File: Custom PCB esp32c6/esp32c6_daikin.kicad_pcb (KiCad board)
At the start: 2 copper layers, 31.6 x 19.8 mm, 35 parts, among them J2 Conn_01x05, Q1 BSS138PS, U1 TPS562246, U2 WT0132C6-S5

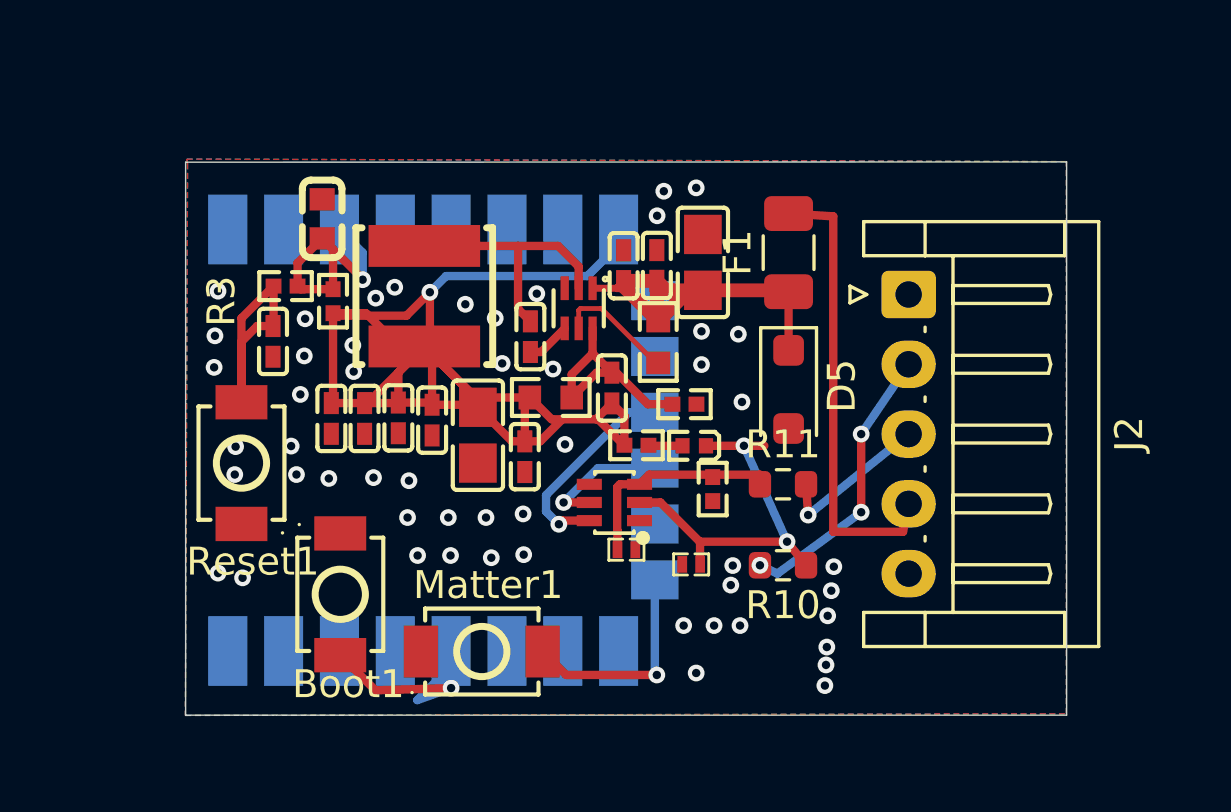
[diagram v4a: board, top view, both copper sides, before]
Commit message: feat(xiao-pcb): place XIAO + kept parts on grown outline
Sync the PCB to the reviewed XIAO-carrier schematic (Task 7, placement only;
routing is Task 8).

- Remove 12 footprints no longer in the netlist (Reset1, Boot1, Matter1, D4,
  R9, C1, C2, C4, C5, C6, C7, C8).
- Swap U2 from the old module footprint (easyeda2kicad:WT0132C6-S5) to the
  Seeed XIAO land pattern (Seeed_XIAO:XIAO-ESP32-C6-DIP).
- Add the 3 new parts: U2 XIAO, D6 (PMEG2005 VBUS Schottky, D_SOD-123),
  C20 (10uF XIAO VBUS decap), R12 (10k). No ferrite (dropped in schematic).
- Reassign every pad net from the exported netlist (89 pads, 0 mismatches,
  full ref-set parity).
- Grow the outline to 40x25 mm. Place U2 on B.Cu at the left short edge with
  the antenna end overhanging (~1mm) and a copper keep-out rule area (no
  tracks / no zone fills, F.Cu+B.Cu) under the antenna. Buck (U1+L1) far end,
  J2 on the right long edge, shifter (Q1/R10/R11) and protection (F1/D5/D6/
  D2/D3) placed accordingly. Courtyard-free R/C nest in the module center gap
  between the two castellated PTH pad rows.
- Delete the stale rev-b routing (209 tracks) and GND pour so the board is
  placed-not-routed.

D5 (SMF15A, unidirectional TVS in a bidirectional symbol): verified at board
level that pad 1 (cathode/band) lands on V_in and pad 2 on GND - correct
clamp polarity.

DRC (kicad-cli 10.0.4): zero footprint/courtyard-overlap, shorting, clearance
or edge-clearance errors; 49 unconnected items expected pre-routing. Remaining
warnings are silkscreen crowding and pre-existing easyeda2kicad lib-table
entries, both non-gating.
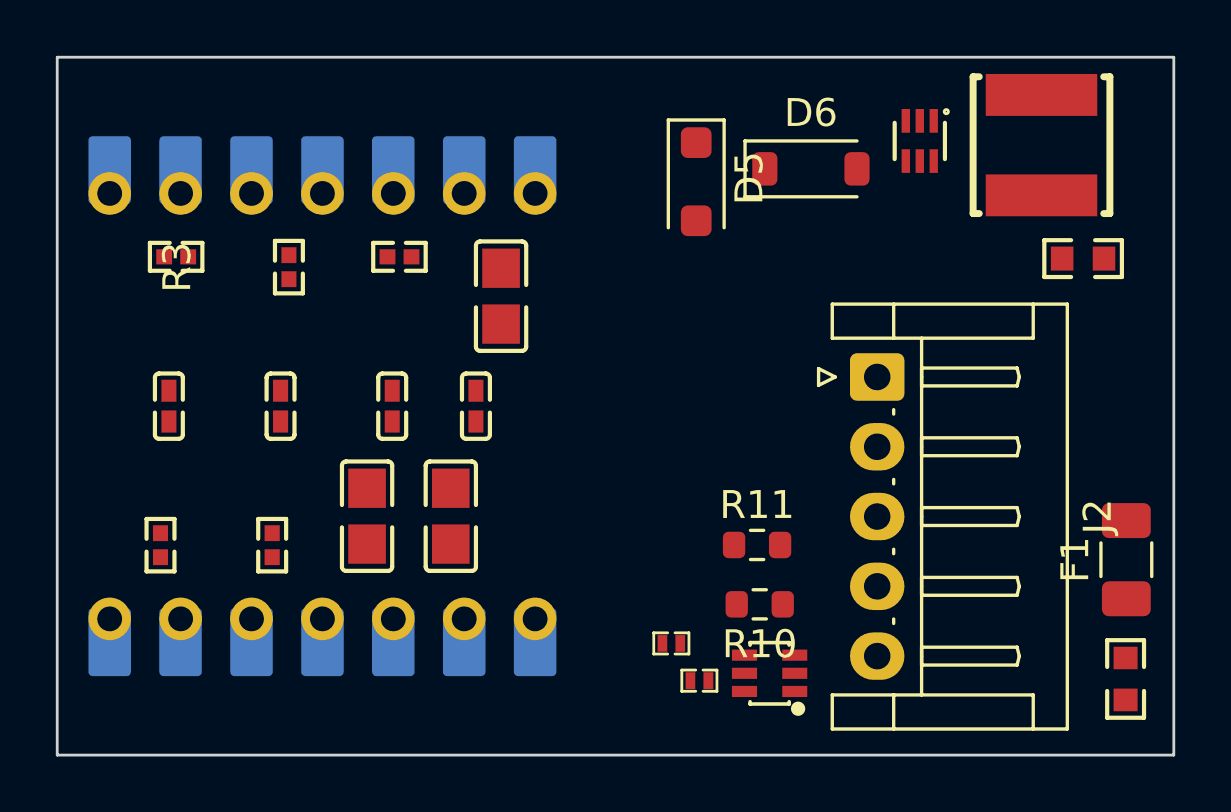
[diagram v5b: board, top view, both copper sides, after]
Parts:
- removed Boot1, Matter1, Reset1: Tactile Button, 160gf, easyeda2kicad:SW-SMD_L3.9-W3.0-P4.45
- removed C1, C2, C4, C5, C7, C8: 100nF, easyeda2kicad:C0402
- removed C6: 1uF, easyeda2kicad:C0603
- removed D4: D, easyeda2kicad:D0402
- removed R9: 220, easyeda2kicad:R0402
- added C20: 10uF 25V, easyeda2kicad:C0805, F.Cu at (164.1, 102.4)
- added D6: PMEG2005, D_SOD-123, F.Cu at (177.0, 90.0)
- added R12: 10k, easyeda2kicad:R0402, F.Cu at (157.7, 103.5)
- U2: value WT0132C6-S5 -> XIAO-ESP32-C6; footprint easyeda2kicad:WT0132C6-S5 -> XIAO-ESP32-C6-DIP
- moved L1 22.8 mm to (185.3, 89.2)
- moved R5 20.6 mm to (188.3, 108.3)
- moved R1 19.9 mm to (153.7, 103.5)
- moved R6 19.7 mm to (186.8, 93.2)
- moved R2 17.8 mm to (154.3, 93.2)
- moved C16 17.0 mm to (154.0, 98.5)
- moved F1 16.4 mm to (188.3, 104.0)
- moved U1 13.6 mm to (180.9, 89.0)
- moved R8 11.5 mm to (162.3, 93.2)
- moved C3 10.7 mm to (162.0, 98.5)
- moved C18 9.29 mm to (158.0, 98.5)
- moved Q1 8.27 mm to (175.5, 108.1)
- moved D5 8.14 mm to (172.9, 90.5)
- moved C17 7.33 mm to (165.9, 94.6)
- moved C15 4.92 mm to (161.1, 102.4)
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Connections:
- C15 pad 1: 3V3 -> /5V_BUCK
- C19 pad 2: 3V3 -> /5V_BUCK
- D2 pad 2: Net-(Q1B-SP) -> /S21_TX_CONN
- D3 pad 2: /S21_TX_CORE -> /S21_RX_CONN
- L1 pad 2: 3V3 -> /5V_BUCK
- Q1 pad 1: GND -> TX1
- Q1 pad 2: /S21_TX_CORE -> 3V3
- Q1 pad 3: Net-(Q1B-SP) -> /HV2
- Q1 pad 4: GND -> RX1
- Q1 pad 5: TX1 -> 3V3
- Q1 pad 6: RX1 -> /HV1
- R1 pad 1: unconnected-(R1-Pad1) -> /5V_BUCK
- R1 pad 2: Net-(Q1B-SP) -> /HV1
- R10 pad 1: /S21_TX_CORE -> /HV1
- R10 pad 2: /S21_TX_CONN -> /S21_RX_CONN
- R11 pad 1: Net-(Q1B-SP) -> /HV2
- R11 pad 2: /S21_RX_CONN -> /S21_TX_CONN
- R2 pad 2: Net-(D4-A) -> TX1
- R3 pad 2: Net-(U2-EN) -> RX1
- R6 pad 1: 3V3 -> /5V_BUCK
- U2 pad 12: Net-(Boot1-A) -> 3V3
- U2 pad 13: unconnected-(U2-GPIO10-Pad13) -> GND
- U2 pad 14: unconnected-(U2-GPIO3-Pad14) -> /VBUS
- U2 pad 3: Net-(U2-EN) -> unconnected-(U2-D2-Pad3)
- U2 pad 7: unconnected-(U2-GPIO6-Pad7) -> TX1
- U2 pad 8: 3V3 -> RX1
- U2 pad 9: GND -> unconnected-(U2-D8-Pad9)
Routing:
- net 3V3: track 53.7 -> 0.00 mm, vias 1 -> 0
- net /12V_IN: track 16.4 -> 0.00 mm
- net V_in: track 14.8 -> 0.00 mm
- net /S21_TX_CORE: track 13.6 -> 0.00 mm, vias 2 -> 0
- net /S21_TX_CONN: track 10.2 -> 0.00 mm, vias 3 -> 0
- net Net-(Reset1-A): track 9.61 -> 0.00 mm
- net Net-(U2-EN): track 9.60 -> 0.00 mm, vias 1 -> 0
- net Net-(U1-SW): track 9.49 -> 0.00 mm
- net Net-(U1-VFB): track 8.21 -> 0.00 mm
- net Net-(Boot1-A): track 8.04 -> 0.00 mm, vias 1 -> 0
- net Net-(Q1B-SP): track 7.89 -> 0.00 mm
- net Net-(Matter1-A): track 7.88 -> 0.00 mm, vias 1 -> 0
- net RX1: track 7.51 -> 0.00 mm, vias 1 -> 0
- net /S21_RX_CONN: track 5.73 -> 0.00 mm, vias 1 -> 0
- net TX1: track 4.70 -> 0.00 mm, vias 1 -> 0
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- removed copper zone on B.Cu, net GND
- removed copper zone on F.Cu, net GND
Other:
- board size 31.6 x 19.8 mm -> 40 x 25 mm

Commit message: fix(xiao-pcb): sync board value fields + footprint lib ids to schematic
Follow-up to 542d1fc, from independent review. The net-level sync propagated
nets and footprints but not component value fields, leaving four parts with
stale rev-b values on the board:

- R6  150k -> 220k   (buck feedback divider; sets Vout)
- R8  33k  -> 30k    (feedforward)
- C19 18pF -> 47pF   (feedforward cap)
- C15 47uF 6V3 -> 47uF 10V  (output cap voltage rating)

These are the Task-5 buck retune values (Vout 5.000 V per TI Table 7-2). A BOM
cut from the PCB would otherwise place the wrong buck parts. Values now match
the schematic netlist for all 26 footprints.

Also set the library nicknames on the two lib-loaded footprints
(U2 -> Seeed_XIAO:XIAO-ESP32-C6-DIP, D6 -> Diode_SMD:D_SOD-123); FootprintLoad
had left them blank. schematic parity was already clean; this is metadata.

DRC unchanged: zero gated (overlap/short/clearance/edge) violations, 49
unconnected (unrouted, expected).
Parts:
- C15: value 47uF 6V3 -> 47uF 10V
- C19: value 18pF -> 47pF
- D6: footprint D_SOD-123 -> Diode_SMD:D_SOD-123
- R6: value 150k 1% -> 220k 1%
- R8: value 33k 1% -> 30k 1%
- U2: footprint XIAO-ESP32-C6-DIP -> Seeed_XIAO:XIAO-ESP32-C6-DIP
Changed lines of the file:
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@@
 		)
 	)
-	(footprint "D_SOD-123"
+	(footprint "Diode_SMD:D_SOD-123"
 		(layer "F.Cu")
 		(at 177 90)
@@
 			)
 		)
-		(property "Value" "18pF"
+		(property "Value" "47pF"
 			(at 0 4 90)
 			(layer "F.Fab")
@@
 			)
 		)
-		(property "Value" "33k 1%"
+		(property "Value" "30k 1%"
 			(at 0 4 0)
 			(layer "F.Fab")
@@
 			)
 		)
-		(property "Value" "150k 1%"
+		(property "Value" "220k 1%"
 			(at 0 4 0)
 			(layer "F.Fab")
@@
 			)
 		)
-		(property "Value" "47uF 6V3"
+		(property "Value" "47uF 10V"
 			(at 0 4 90)
 			(layer "F.Fab")
@@
 		)
 	)
-	(footprint "XIAO-ESP32-C6-DIP"
+	(footprint "Seeed_XIAO:XIAO-ESP32-C6-DIP"
 		(layer "B.Cu")
 		(at 159.5 98.5)
